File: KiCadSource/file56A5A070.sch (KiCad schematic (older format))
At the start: 81 parts, among them U19 SPX3819, U20 MAX15053, U21 MAX15053, U22 MAX15053, U23 MCP4251, U24 LM2776, U25 MAX15053, U26 MAX15053, U27 SPX3819, U28 TPS72301

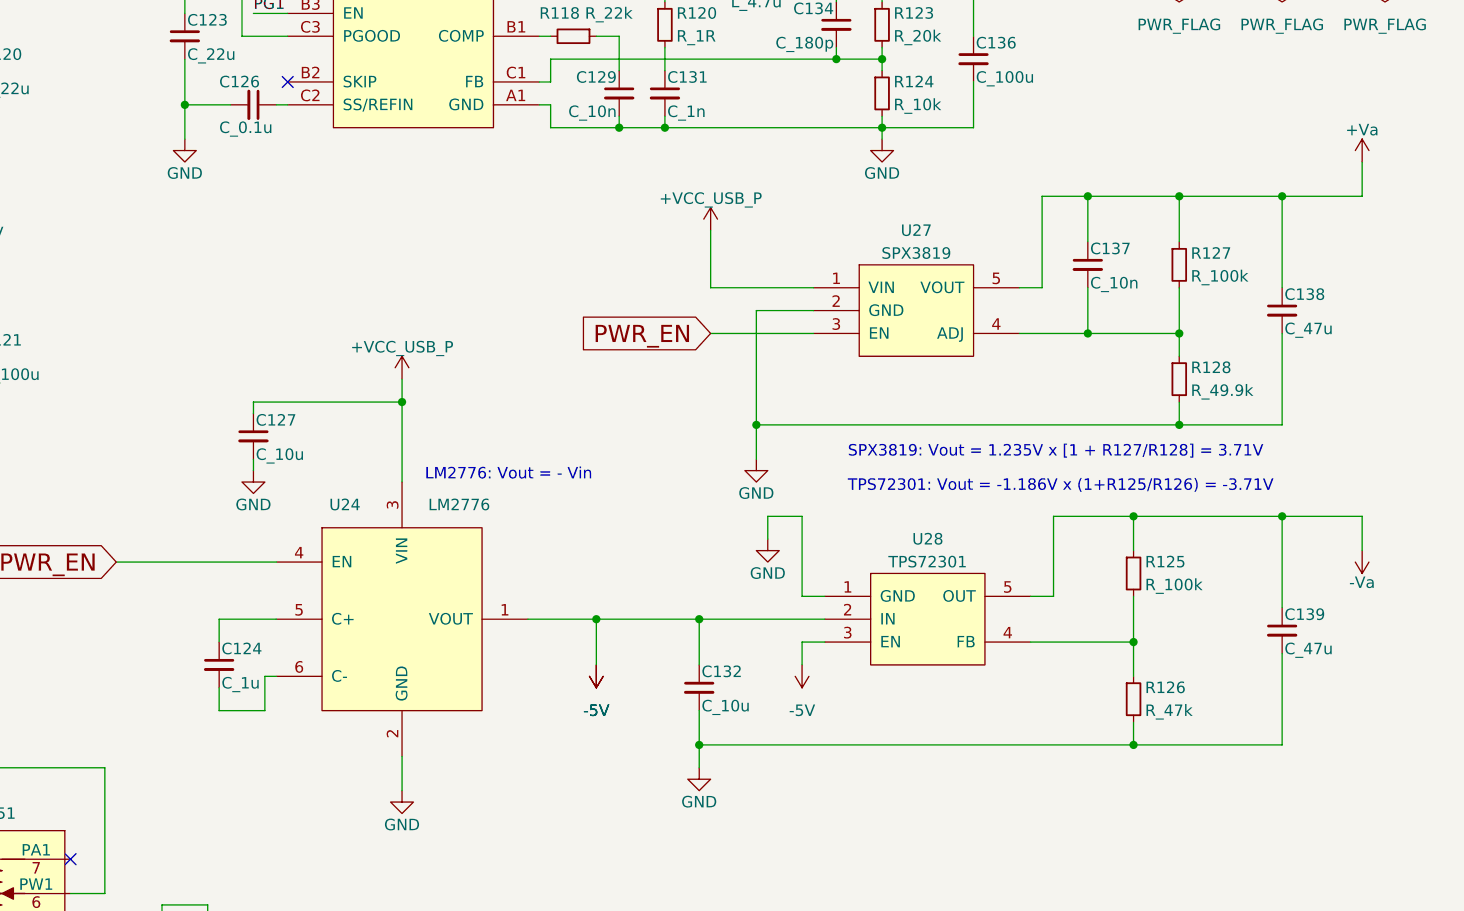
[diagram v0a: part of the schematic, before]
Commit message: first production run, digital GPIOs, replaced parts (see CHANGES.txt)
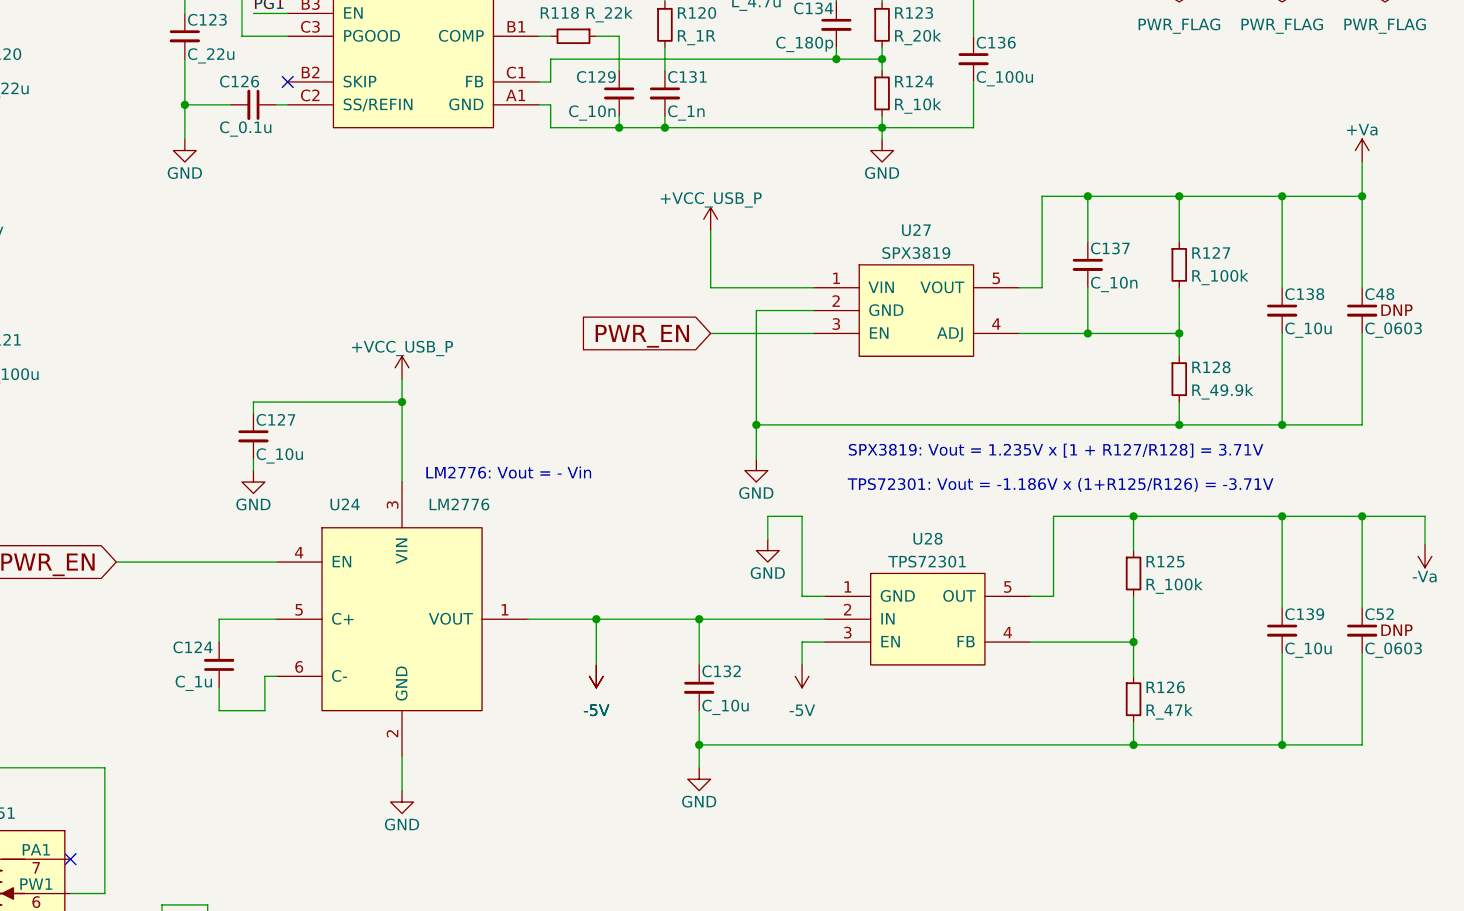
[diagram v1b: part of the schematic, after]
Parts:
- removed C138, C139: C_47u, ScopefunPackagesLibrary:C_1210, symbol C_47u
- added C138, C139: C_10u, ScopefunPackagesLibrary:C_0603, symbol C_10u
- added C48, C52: C_0603, ScopefunPackagesLibrary:C_0603, symbol C_0603
- C124: Description MLCC - SMD/SMT 0603 10V X7R 10% -> MLCC - SMD/SMT 0603 6.3V X5R 10%
- C127, C132: Description MLCC - SMD/SMT 0603 6.3V X5R 20% -> MLCC - SMD/SMT 0603 6.3V X5R 10%
- U23: Description Dual Digital Potentiometer 100kOhm -> Dual Digital Potentiometer 50kOhm
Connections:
- net -Va: now also C139.1, C52.1
- net GND: now also C138.2, C139.2, C48.2, C52.2
- net Va: now also C138.1, C48.1
- net at C124.1: now also U24.6 (C-); no longer U24.5 (C+)
- net at C124.2: now also U24.5 (C+); no longer U24.6 (C-)
